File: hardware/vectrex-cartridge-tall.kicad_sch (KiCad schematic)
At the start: 18 parts

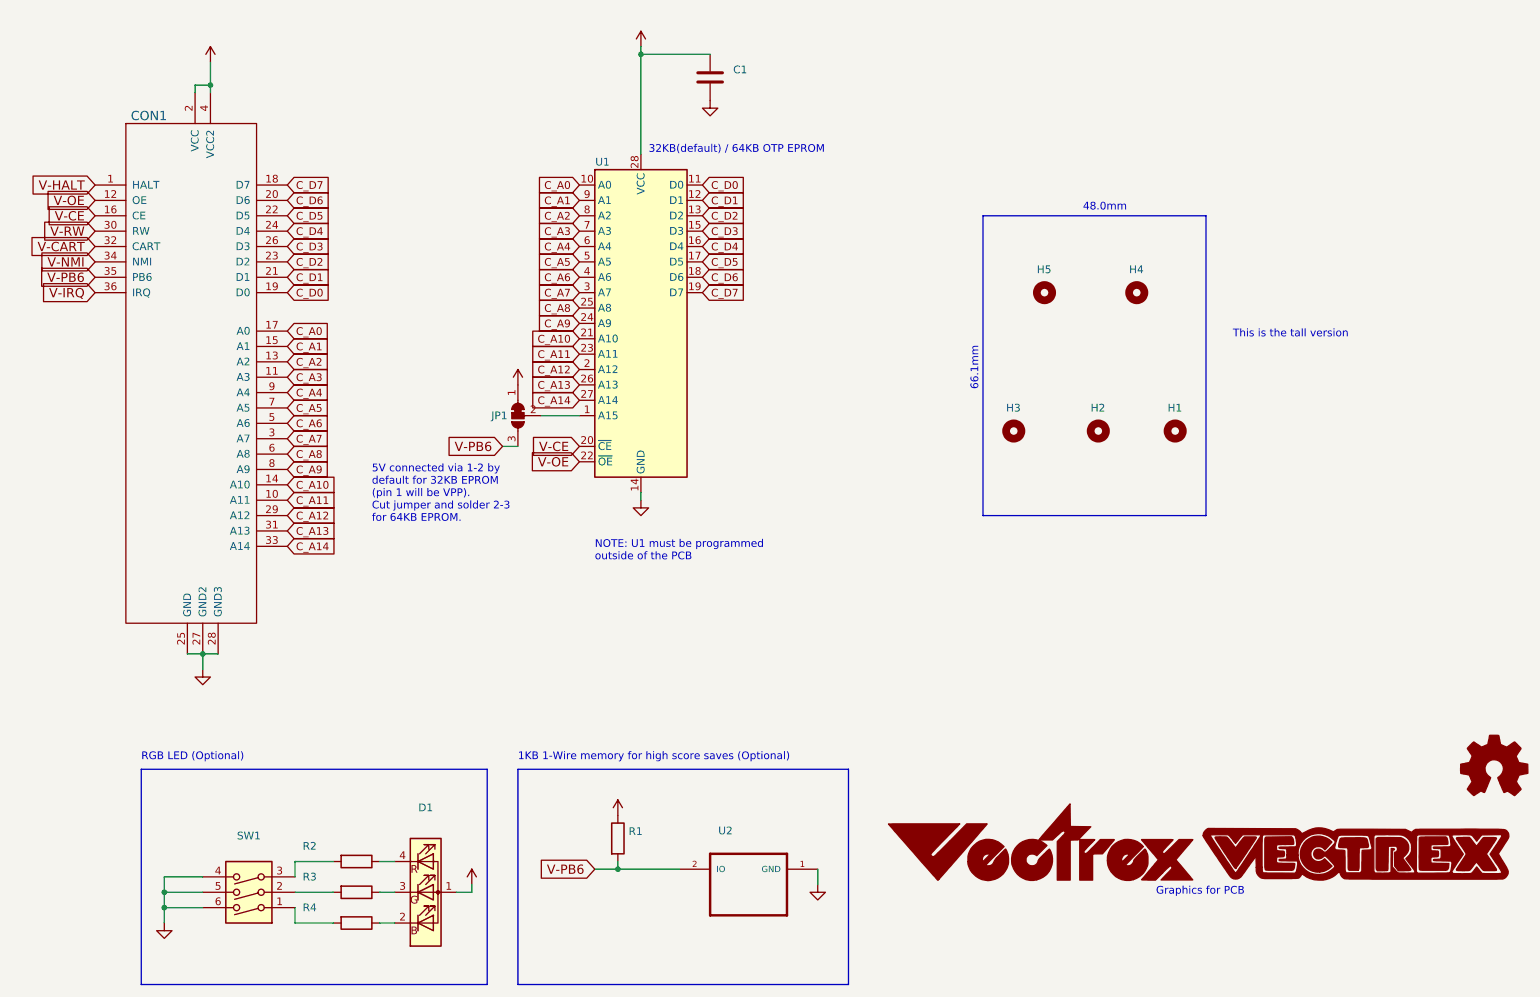
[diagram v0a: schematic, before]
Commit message: update RGB LED resistor values for deeper color
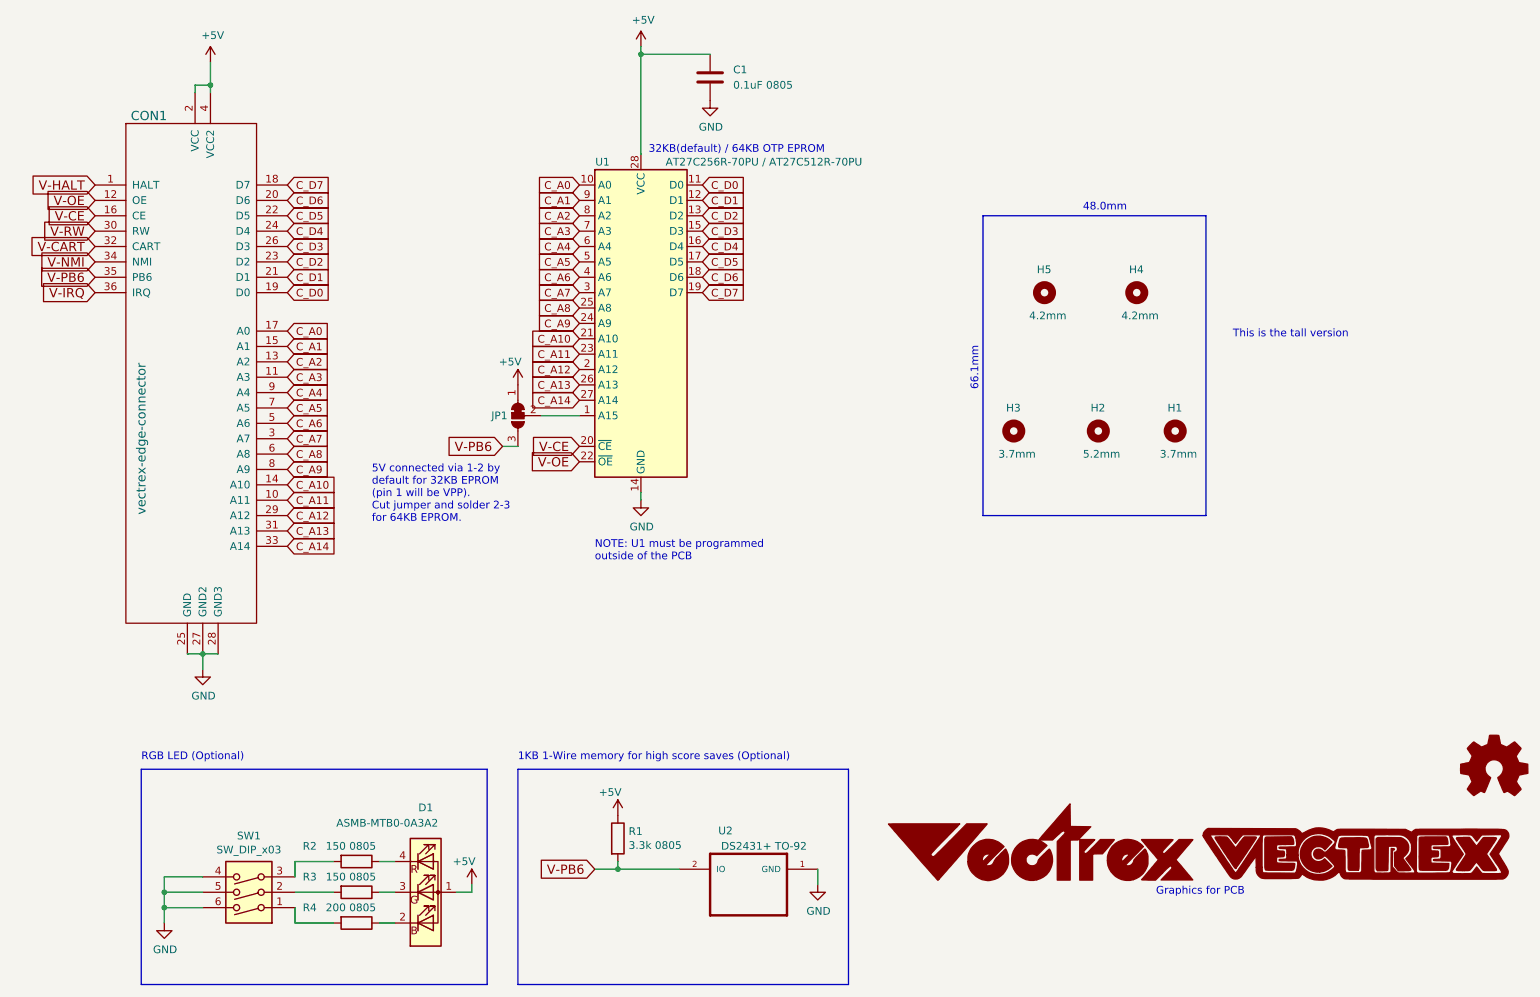
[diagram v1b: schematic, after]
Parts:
- C1: value (none) -> 0.1uF 0805; footprint (none) -> Capacitor_SMD:C_0805_2012Metric_Pad1.15x1.40mm_HandSolder
- CON1: value (none) -> vectrex-edge-connector; footprint (none) -> vectrex-cartridge:vectrex-edge-connector-thinner-no-soldermask
- D1: value (none) -> ASMB-MTB0-0A3A2; footprint (none) -> vectrex-cartridge:LED_Avago_PLCC4_3.2x2.8mm_CW
- G1: value (none) -> LOGO; footprint (none) -> vectrex-cartridge:vectrex-us-soldermask
- G3: value (none) -> LOGO; footprint (none) -> vectrex-cartridge:vectrex-uk-soldermask
- H1, H3: value (none) -> 3.7mm; footprint (none) -> vectrex-cartridge:Mounting_Hole_D3.7mm
- H2: value (none) -> 5.2mm; footprint (none) -> vectrex-cartridge:Mounting_Hole_D5.2mm
- H4, H5: value (none) -> 4.2mm; footprint (none) -> vectrex-cartridge:Mounting_Hole_D4.2mm
- JP1: value (none) -> SolderJumper_3_Bridged12; footprint (none) -> vectrex-cartridge:SolderJumper-3_P1.3mm_Bridged12_RoundedPad1.0x1.5mm_NumberLabels
- R1: value (none) -> 3.3k 0805; footprint (none) -> Resistor_SMD:R_0805_2012Metric_Pad1.15x1.40mm_HandSolder
- R2, R3: value (none) -> 150 0805; footprint (none) -> Resistor_SMD:R_0805_2012Metric_Pad1.15x1.40mm_HandSolder
- R4: value (none) -> 200 0805; footprint (none) -> Resistor_SMD:R_0805_2012Metric_Pad1.15x1.40mm_HandSolder
- SW1: value (none) -> SW_DIP_x03; footprint (none) -> Button_Switch_SMD:SW_DIP_SPSTx03_Slide_6.7x9.18mm_W8.61mm_P2.54mm_LowProfile
- U1: value (none) -> AT27C256R-70PU / AT27C512R-70PU; footprint (none) -> Package_DIP:DIP-28_W15.24mm
- U2: value (none) -> DS2431+ TO-92; footprint (none) -> vectrex-cartridge:TO-92_Inline_BW
